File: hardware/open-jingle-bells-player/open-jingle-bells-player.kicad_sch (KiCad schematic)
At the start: 50 parts, among them J1 USB_C, J2 Music_Module, J3 UART, Q1 AO3401A, Q2 2N7002, U1 ESP32-S3-WROOM-1-N8, U2 AZ1117-3.3, U4 USBLC6-2SC6, U5 TXS0108EPW, U6 TXS0108EPW, U7 TXS0108EPW

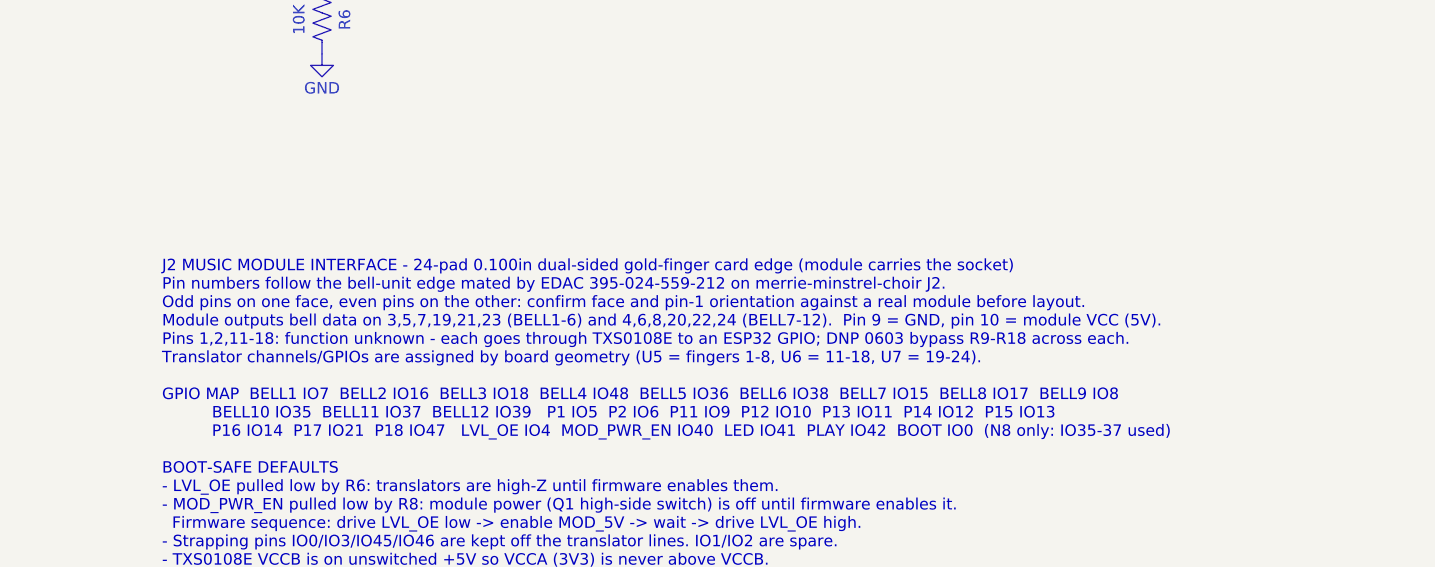
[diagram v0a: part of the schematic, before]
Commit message: Rename the project to Open Jingle Bells
The KiCad projects become open-jingle-bells-choir and
open-jingle-bells-player, the tools package becomes
open-jingle-bells-tools with ojb-* commands, and the firmware's page,
setup AP (JingleBells-XXXX) and default host name take the new name.
The NVS namespace stays "minstrel" so flashed units keep their settings.

Co-Authored-By: Claude Opus 5.5 <noreply@anthropic.com>
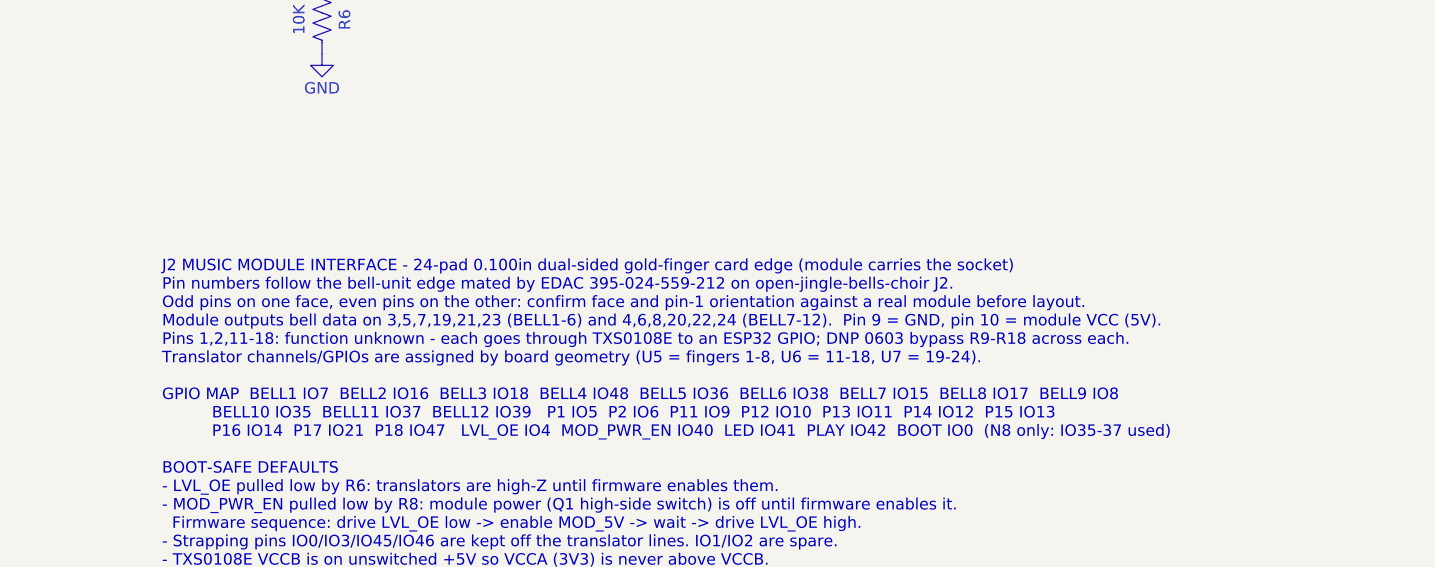
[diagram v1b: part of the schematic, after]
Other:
- note added: "J2 MUSIC MODULE INTERFACE - 24-pad 0.100in dual-sided gold-finger card edge (module carries the socket) Pin numbers follow the bell-unit edge mated by EDAC 395-024-559-212 on open-jingle-bells-choir J2. Odd pins on one face, even pins on the other: confirm face and pin-1 orientation against a real module before layout. Module outputs bell data on 3,5,7,19,21,23 (BELL1-6) and 4,6,8,20,22,24 (BELL7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"
- note removed: "J2 MUSIC MODULE INTERFACE - 24-pad 0.100in dual-sided gold-finger card edge (module carries the socket) Pin numbers follow the bell-unit edge mated by EDAC 395-024-559-212 on merrie-minstrel-choir J2. Odd pins on one face, even pins on the other: confirm face and pin-1 orientation against a real module before layout. Module outputs bell data on 3,5,7,19,21,23 (BELL1-6) and 4,6,8,20,22,24 (BELL7-1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"
